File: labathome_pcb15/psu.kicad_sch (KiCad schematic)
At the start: 38 parts, among them J8 POWER, J9 Barrel_Jack_Switch, SW11 PROG 5V POWER, SW4 BATT POWER, SW5 POWER, U11 AMS1117, U2 IP5306_I2C, U24 SRV05, U27 TPS54202DDC

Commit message: 4 Layers
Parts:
- C1, C4: footprint Capacitor_SMD:C_0603_1608Metric -> Capacitor_SMD:C_0805_2012Metric
- C80: footprint Capacitor_SMD:C_1206_3216Metric -> Capacitor_SMD:C_0805_2012Metric
- R48: footprint Resistor_SMD:R_0201_0603Metric -> Resistor_SMD:R_0402_1005Metric
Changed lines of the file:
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@@
 			)
 		)
-		(property "Footprint" "Resistor_SMD:R_0201_0603Metric"
+		(property "Footprint" "Resistor_SMD:R_0402_1005Metric"
 			(at 88.138 124.46 90)
 			(effects
@@
 			)
 		)
-		(property "Footprint" "Capacitor_SMD:C_0603_1608Metric"
+		(property "Footprint" "Capacitor_SMD:C_0805_2012Metric"
 			(at 122.8852 55.88 0)
 			(effects
@@
 			)
 		)
-		(property "Footprint" "Capacitor_SMD:C_1206_3216Metric"
+		(property "Footprint" "Capacitor_SMD:C_0805_2012Metric"
 			(at 24.4348 109.22 0)
 			(effects
@@
 			)
 		)
-		(property "Footprint" "Capacitor_SMD:C_0603_1608Metric"
+		(property "Footprint" "Capacitor_SMD:C_0805_2012Metric"
 			(at 133.0452 48.26 0)
 			(effects

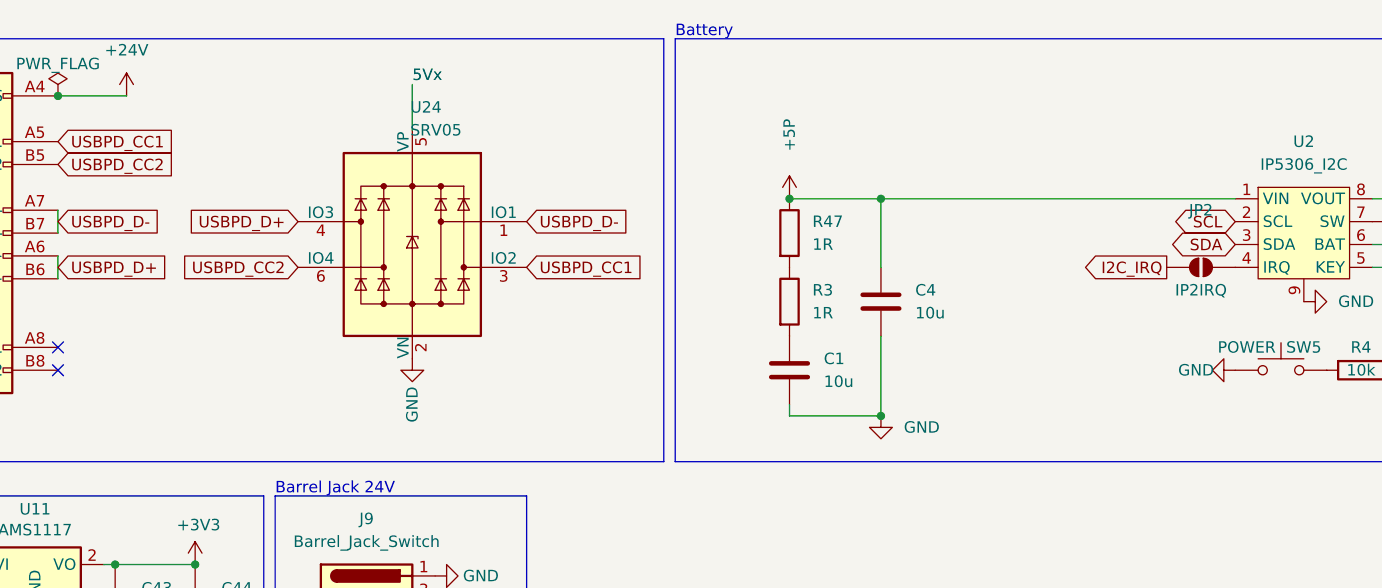
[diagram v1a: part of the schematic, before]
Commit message: 4layer board improvement
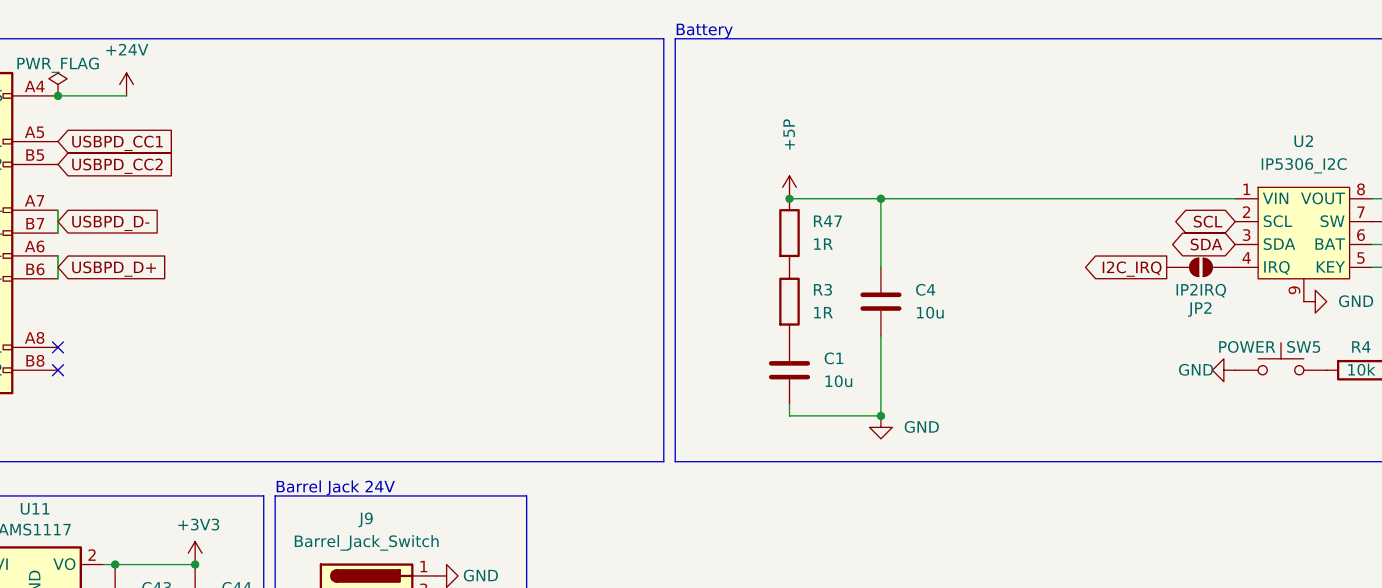
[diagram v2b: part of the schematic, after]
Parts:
- removed U24: SRV05, Package_TO_SOT_SMD:SOT-23-6, symbol Power_Protection:SRV05-4

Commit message: IP5306
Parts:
- removed JP2: IP2IRQ, Jumper:SolderJumper-2_P1.3mm_Open_RoundedPad1.0x1.5mm, symbol Jumper:SolderJumper_2_Open
- SW4: value BATT POWER -> LOAD POWERBANK
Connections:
- net +5V: no longer SW4.1 (A)
- net +5VL: now reaches C28.2, C30.2, C31.2, U2.8 (VOUT)
- net +5VL: now also SW11.3 (C), SW4.3 (C); no longer SW4.2 (B)
- net +5P: no longer names the net of C4.1, R47.1, U2.1 (VIN)
- net +5P: now also SW4.1 (A); no longer SW11.3 (C)
- new net 5V_USB: SW4.2 (B)

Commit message: bsec
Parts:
- removed SW11: PROG 5V POWER, liebler_MECH:Switch_SS12D00, symbol Switch:SW_SPDT
- removed SW4: LOAD POWERBANK, liebler_MECH:Switch_SS12D00, symbol Switch:SW_SPDT
- added J29: PowerBank, liebler_CONN:USB_C_Receptacle_HRO_TYPE-C-31-M-12_IMPROVED, symbol Connector:USB_C_Receptacle_USB2.0_16P
- added R72: 10k, Resistor_SMD:R_0201_0603Metric, symbol Device:R
- added R73: 3k3, Resistor_SMD:R_0402_1005Metric, symbol Device:R
- added U18: TPS2116DRL, Package_TO_SOT_SMD:SOT-583-8, symbol Power_Management:TPS2116DRL
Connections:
- net +5V: now also J29.A4 (VBUS), J29.A9 (VBUS), J29.B4 (VBUS), J29.B9 (VBUS), U18.2 (VOUT), U18.7 (VOUT)
- net +5VL: now also U18.6 (VIN2)
- net 5V_USB: now also C4.1, R47.1, U2.1 (VIN)
- net 5Vx: now also R72.1, U18.3 (VIN1), U18.5 (MODE)
- net GND: now also J29.A1 (GND), J29.A12 (GND), J29.B1 (GND), J29.B12 (GND), J29.S1 (SHIELD), R73.1, U18.1 (GND)
- new net: R72.2, R73.2, U18.4 (PR1)
- no-connect marks 5 -> 6

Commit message: TPS2116
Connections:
- net +5V: now also C28.2, C30.2, C31.2, U2.8 (VOUT); no longer U18.2 (VOUT), U18.7 (VOUT)
- net 5V_USB: now also U18.6 (VIN2); no longer C4.1, R47.1, U2.1 (VIN)
- net at R73.2, U18.4 (PR1): now also R72.1; no longer R72.2
- removed net +5VL: C28.2, C30.2, C31.2, U18.6 (VIN2), U2.8 (VOUT)
- net 5Vx renamed 5V_PD
- net 5V_PD: now also R72.2; no longer R72.1
- new net: C4.1, R47.1, U18.2 (VOUT), U18.7 (VOUT), U2.1 (VIN)
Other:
- moved on the sheet: C1, C4, R3, R47, R72, R73, U18

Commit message: Fixes for 15.2 and 15.ß
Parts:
- added JP2: 5V DIR, Jumper:SolderJumper-2_P1.3mm_Bridged2Bar_Pad1.0x1.5mm, symbol Jumper:Jumper_2_Bridged
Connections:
- net +5V: now also JP2.2 (B)
- net at C4.1, R47.1, U18.2 (VOUT)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: now also JP2.1 (A)
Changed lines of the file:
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@@
 	)
 	(junction
+		(at 187.96 33.02)
+		(diameter 0)
+		(color 0 0 0 0)
+	)
+	(junction
 		(at 38.1 81.28)
 		(diameter 0)
@@
 	(wire
 		(pts
+			(xy 158.75 22.86) (xy 158.75 33.02)
+		)
+		(stroke
+			(width 0)
+			(type default)
+		)
+	)
+	(wire
+		(pts
+			(xy 187.96 22.86) (xy 187.96 33.02)
+		)
+		(stroke
+			(width 0)
+			(type default)
+		)
+	)
+	(wire
+		(pts
 			(xy 110.49 27.94) (xy 120.65 27.94)
 		)
@@
 	(wire
 		(pts
-			(xy 186.69 33.02) (xy 199.39 33.02)
+			(xy 173.99 22.86) (xy 158.75 22.86)
+		)
+		(stroke
+			(width 0)
+			(type default)
+		)
+	)
+	(wire
+		(pts
+			(xy 187.96 33.02) (xy 199.39 33.02)
+		)
+		(stroke
+			(width 0)
+			(type default)
+		)
+	)
+	(wire
+		(pts
+			(xy 186.69 33.02) (xy 187.96 33.02)
 		)
 		(stroke
@@
 	(wire
 		(pts
+			(xy 184.15 22.86) (xy 187.96 22.86)
+		)
+		(stroke
+			(width 0)
+			(type default)
+		)
+	)
+	(wire
+		(pts
 			(xy 100.33 113.03) (xy 100.33 128.27)
 		)
@@
 					(unit 1)
 				)
+			)
+		)
+	)
+	(symbol
+		(lib_id "Jumper:Jumper_2_Bridged")
+		(at 179.07 22.86 0)
+		(unit 1)
+		(exclude_from_sim yes)
+		(in_bom yes)
+		(on_board yes)
+		(dnp no)
+		(fields_autoplaced yes)
+		(property "Reference" "JP2"
+			(at 179.07 17.78 0)
+			(effects
+				(font
+					(size 1.27 1.27)
+				)
+			)
+		)
+		(property "Value" "5V DIR"
+			(at 179.07 20.32 0)
+			(effects
+				(font
+					(size 1.27 1.27)
+				)
+			)
+		)
+		(property "Footprint" "Jumper:SolderJumper-2_P1.3mm_Bridged2Bar_Pad1.0x1.5mm"
+			(at 179.07 22.86 0)
+			(effects
+				(font
+					(size 1.27 1.27)
+				)
+				(hide yes)
+			)
+		)
+		(property "Datasheet" "~"
+			(at 179.07 22.86 0)
+			(effects
+				(font
+					(size 1.27 1.27)
+				)
+				(hide yes)
+			)
+		)
+		(property "Description" "Jumper, 2-pole, closed/bridged"
+			(at 179.07 22.86 0)
+			(effects
+				(font
+					(size 1.27 1.27)
+				)
+				(hide yes)
+			)
+		)
+		(pin "2"
+		)
+		(pin "1"
+		)
+		(instances
+			(project ""
+				(path "/e4d6926a-1a8b-424d-97c4-66b6ad87e4ac/77dfbe0c-d674-478a-bf0e-cfa040fb2e8f"
+					(reference "JP2")
+					(unit 1)
+				)

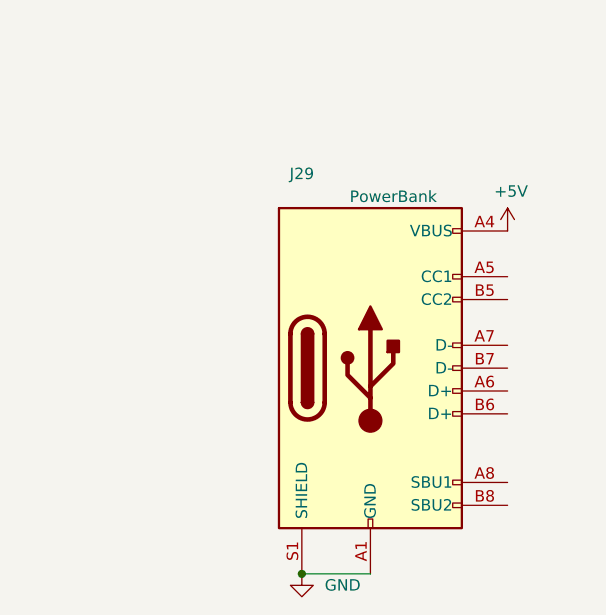
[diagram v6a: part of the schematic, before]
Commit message: Added stepper, no DRC errors, not yet optimized
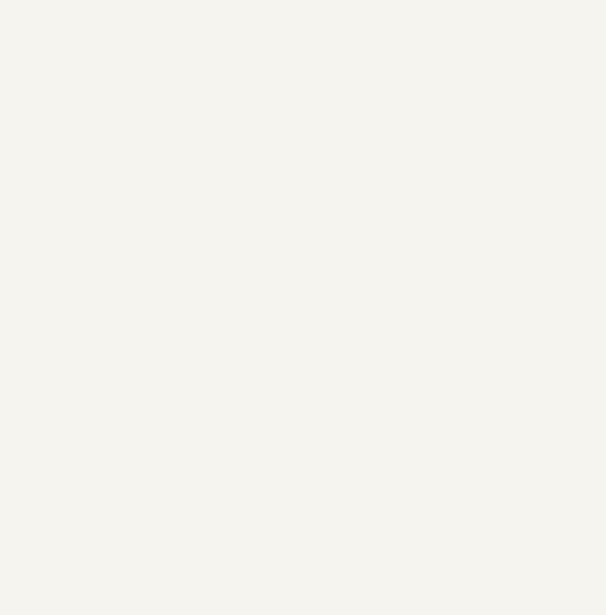
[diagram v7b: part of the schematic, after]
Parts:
- removed J29: PowerBank, liebler_CONN:USB_C_Receptacle_HRO_TYPE-C-31-M-12_IMPROVED, symbol Connector:USB_C_Receptacle_USB2.0_16P
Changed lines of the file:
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@@
 	)
 	(junction
-		(at 200.66 128.27)
-		(diameter 0)
-		(color 0 0 0 0)
-	)
-	(junction
 		(at 90.17 128.27)
 		(diameter 0)
@@
 	(wire
 		(pts
-			(xy 200.66 128.27) (xy 208.28 128.27)
-		)
-		(stroke
-			(width 0)
-			(type default)
-		)
-	)
-	(wire
-		(pts
 			(xy 100.33 128.27) (xy 90.17 128.27)
 		)
@@
 	)
 	(symbol
-		(lib_id "power:+5V")
-		(at 223.52 90.17 0)
-		(unit 1)
-		(exclude_from_sim no)
-		(in_bom yes)
-		(on_board yes)
-		(dnp no)
-		(property "Reference" "#PWR035"
-			(at 223.52 93.98 0)
-			(effects
-				(font
-					(size 1.27 1.27)
-				)
-				(hide yes)
-			)
-		)
-		(property "Value" "+5V"
-			(at 223.901 85.7758 0)
-			(effects
-				(font
-					(size 1.27 1.27)
-				)
-			)
-		)
-		(property "Footprint" ""
-			(at 223.52 90.17 0)
-			(effects
-				(font
-					(size 1.27 1.27)
-				)
-				(hide yes)
-			)
-		)
-		(property "Datasheet" ""
-			(at 223.52 90.17 0)
-			(effects
-				(font
-					(size 1.27 1.27)
-				)
-				(hide yes)
-			)
-		)
-		(property "Description" "Power symbol creates a global label with name \"+5V\""
-			(at 223.52 90.17 0)
-			(effects
-				(font
-					(size 1.27 1.27)
-				)
-				(hide yes)
-			)
-		)
-		(pin "1"
-		)
-		(instances
-			(project "labathome_pcb15"
-				(path "/e4d6926a-1a8b-424d-97c4-66b6ad87e4ac/77dfbe0c-d674-478a-bf0e-cfa040fb2e8f"
-					(reference "#PWR035")
-					(unit 1)
-				)
-			)
-		)
-	)
-	(symbol
 		(lib_id "Device:C")
 		(at 90.17 109.22 0)
@@
 	)
 	(symbol
-		(lib_id "Connector:USB_C_Receptacle_USB2.0_16P")
-		(at 208.28 105.41 0)
-		(unit 1)
-		(exclude_from_sim no)
-		(in_bom yes)
-		(on_board yes)
-		(dnp no)
-		(property "Reference" "J29"
-			(at 200.66 83.82 0)
-			(effects
-				(font
-					(size 1.27 1.27)
-				)
-			)
-		)
-		(property "Value" "PowerBank"
-			(at 210.82 86.36 0)
-			(effects
-				(font
-					(size 1.27 1.27)
-				)
-			)
-		)
-		(property "Footprint" "liebler_CONN:USB_C_Receptacle_HRO_TYPE-C-31-M-12_IMPROVED"
-			(at 212.09 105.41 0)
-			(effects
-				(font
-					(size 1.27 1.27)
-				)
-				(hide yes)
-			)
-		)
-		(property "Datasheet" "https://www.usb.org/sites/default/files/documents/usb_type-c.zip"
-			(at 212.09 105.41 0)
-			(effects
-				(font
-					(size 1.27 1.27)
-				)
-				(hide yes)
-			)
-		)
-		(property "Description" "USB 2.0-only 16P Type-C Receptacle connector"
-			(at 208.28 105.41 0)
-			(effects
-				(font
-					(size 1.27 1.27)
-				)
-				(hide yes)
-			)
-		)
-		(pin "A1"
-		)
-		(pin "A12"
-		)
-		(pin "A4"
-		)
-		(pin "A5"
-		)
-		(pin "A6"
-		)
-		(pin "A7"
-		)
-		(pin "A8"
-		)
-		(pin "A9"
-		)
-		(pin "B1"
-		)
-		(pin "B12"
-		)
-		(pin "B4"
-		)
-		(pin "B5"
-		)
-		(pin "B6"
-		)
-		(pin "B7"
-		)
-		(pin "B8"
-		)
-		(pin "B9"
-		)
-		(pin "S1"
-		)
-		(instances
-			(project "labathome_pcb15"
-				(path "/e4d6926a-1a8b-424d-97c4-66b6ad87e4ac/77dfbe0c-d674-478a-bf0e-cfa040fb2e8f"
-					(reference "J29")
-					(unit 1)
-				)
-			)
-		)
-	)
-	(symbol
 		(lib_id "Device:C")
 		(at 208.28 46.99 0)
@@
 					(unit 1)
 				)
-			)
-		)
-	)
-	(symbol
-		(lib_id "power:GND")
-		(at 200.66 128.27 0)
-		(unit 1)
-		(exclude_from_sim no)
-		(in_bom yes)
-		(on_board yes)
-		(dnp no)
-		(fields_autoplaced yes)
-		(property "Reference" "#PWR050"
-			(at 200.66 134.62 0)
-			(effects
-				(font
-					(size 1.27 1.27)
-				)
-				(hide yes)
-			)
-		)
-		(property "Value" "GND"
-			(at 203.2 129.5399 0)
-			(effects
-				(font
-					(size 1.27 1.27)
-				)
-				(justify left)
-			)
-		)
-		(property "Footprint" ""
-			(at 200.66 128.27 0)
-			(effects
-				(font
-					(size 1.27 1.27)
-				)
-				(hide yes)
-			)
-		)
-		(property "Datasheet" ""
-			(at 200.66 128.27 0)
-			(effects
-				(font
-					(size 1.27 1.27)
-				)
-				(hide yes)
-			)
-		)
-		(property "Description" "Power symbol creates a global label with name \"GND\" , ground"
-			(at 200.66 128.27 0)
-			(effects
-				(font
-					(size 1.27 1.27)
-				)
-				(hide yes)
-			)
-		)
-		(pin "1"
-		)
-		(instances
-			(project "labathome_pcb15"
-				(path "/e4d6926a-1a8b-424d-97c4-66b6ad87e4ac/77dfbe0c-d674-478a-bf0e-cfa040fb2e8f"
-					(reference "#PWR050")
-					(unit 1)
-				)
